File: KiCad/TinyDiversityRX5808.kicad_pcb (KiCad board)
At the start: 2 copper layers, 22 x 19.7 mm, 31 parts, among them J1 Googles, J2 RX_A, J3 RX_B, J4 Conn_01x06, SW1 SW_Push, U1 MAX4624, U2 ATTINY85-20SU

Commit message: Change schottky footprint
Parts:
- D3: footprint Diodes_SMD:D_SOD-523 -> Diodes_SMD:D_SOD-323
- moved D3 0.30 mm to (148.9, 94.9)
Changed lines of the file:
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@@
-    )
-  )
-  (module Diodes_SMD:D_SOD-523 (layer F.Cu)
-    (at 148.65 94.83)
-    (descr "http://www.diodes.com/datasheets/ap02001.pdf p.144")
-    (tags "Diode SOD523")
-    (attr smd)
-    (fp_text reference D3 (at 0 -1.3) (layer F.SilkS) hide
-      (effects (font (size 1 1) (thickness 0.15)))
-    )
-    (fp_text value D_Schottky (at 0 1.4) (layer F.Fab) hide
-      (effects (font (size 1 1) (thickness 0.15)))
-    )
-    (fp_text user %R (at 0 -1.3) (layer F.Fab) hide
-      (effects (font (size 1 1) (thickness 0.15)))
-    )
-    (fp_line (start -1.15 -0.6) (end -1.15 0.6) (layer F.SilkS) (width 0.12))
-    (fp_line (start 1.25 -0.7) (end 1.25 0.7) (layer F.CrtYd) (width 0.05))
-    (fp_line (start -1.25 -0.7) (end 1.25 -0.7) (layer F.CrtYd) (width 0.05))
-    (fp_line (start -1.25 0.7) (end -1.25 -0.7) (layer F.CrtYd) (width 0.05))
-    (fp_line (start 1.25 0.7) (end -1.25 0.7) (layer F.CrtYd) (width 0.05))
-    (fp_line (start 0.1 0) (end 0.25 0) (layer F.Fab) (width 0.1))
-    (fp_line (start 0.1 -0.2) (end -0.2 0) (layer F.Fab) (width 0.1))
-    (fp_line (start 0.1 0.2) (end 0.1 -0.2) (layer F.Fab) (width 0.1))
-    (fp_line (start -0.2 0) (end 0.1 0.2) (layer F.Fab) (width 0.1))
-    (fp_line (start -0.2 0) (end -0.35 0) (layer F.Fab) (width 0.1))
-    (fp_line (start -0.2 0.2) (end -0.2 -0.2) (layer F.Fab) (width 0.1))
-    (fp_line (start 0.65 -0.45) (end 0.65 0.45) (layer F.Fab) (width 0.1))
-    (fp_line (start -0.65 -0.45) (end 0.65 -0.45) (layer F.Fab) (width 0.1))
-    (fp_line (start -0.65 0.45) (end -0.65 -0.45) (layer F.Fab) (width 0.1))
-    (fp_line (start 0.65 0.45) (end -0.65 0.45) (layer F.Fab) (width 0.1))
-    (fp_line (start 0.7 -0.6) (end -1.15 -0.6) (layer F.SilkS) (width 0.12))
-    (fp_line (start 0.7 0.6) (end -1.15 0.6) (layer F.SilkS) (width 0.12))
-    (pad 2 smd rect (at 0.7 0 180) (size 0.6 0.7) (layers F.Cu F.Paste F.Mask)
-      (net 3 VCC))
-    (pad 1 smd rect (at -0.7 0 180) (size 0.6 0.7) (layers F.Cu F.Paste F.Mask)
-      (net 2 /PROG_PWR))
-    (model ${KISYS3DMOD}/Diodes_SMD.3dshapes/D_SOD-523.wrl
-      (at (xyz 0 0 0))
-      (scale (xyz 1 1 1))
-      (rotate (xyz 0 0 0))
     )
   )
@@
       (scale (xyz 1 1 1))
       (rotate (xyz 0 0 180))
+    )
+  )
+  (module Diodes_SMD:D_SOD-323 (layer F.Cu)
+    (at 148.93 94.93)
+    (descr SOD-323)
+    (tags SOD-323)
+    (attr smd)
+    (fp_text reference D3 (at 1.07 -1.43) (layer F.SilkS) hide
+      (effects (font (size 0.6 0.6) (thickness 0.15)))
+    )
+    (fp_text value D_Schottky (at 0.1 1.9) (layer F.Fab) hide
+      (effects (font (size 1 1) (thickness 0.15)))
+    )
+    (fp_text user %R (at 3.14 -0.26) (layer F.Fab) hide
+      (effects (font (size 1 1) (thickness 0.15)))
+    )
+    (fp_line (start -1.5 -0.85) (end -1.5 0.85) (layer F.SilkS) (width 0.12))
+    (fp_line (start 0.2 0) (end 0.45 0) (layer F.Fab) (width 0.1))
+    (fp_line (start 0.2 0.35) (end -0.3 0) (layer F.Fab) (width 0.1))
+    (fp_line (start 0.2 -0.35) (end 0.2 0.35) (layer F.Fab) (width 0.1))
+    (fp_line (start -0.3 0) (end 0.2 -0.35) (layer F.Fab) (width 0.1))
+    (fp_line (start -0.3 0) (end -0.5 0) (layer F.Fab) (width 0.1))
+    (fp_line (start -0.3 -0.35) (end -0.3 0.35) (layer F.Fab) (width 0.1))
+    (fp_line (start -0.9 0.7) (end -0.9 -0.7) (layer F.Fab) (width 0.1))
+    (fp_line (start 0.9 0.7) (end -0.9 0.7) (layer F.Fab) (width 0.1))
+    (fp_line (start 0.9 -0.7) (end 0.9 0.7) (layer F.Fab) (width 0.1))
+    (fp_line (start -0.9 -0.7) (end 0.9 -0.7) (layer F.Fab) (width 0.1))
+    (fp_line (start -1.6 -0.95) (end 1.6 -0.95) (layer F.CrtYd) (width 0.05))
+    (fp_line (start 1.6 -0.95) (end 1.6 0.95) (layer F.CrtYd) (width 0.05))
+    (fp_line (start -1.6 0.95) (end 1.6 0.95) (layer F.CrtYd) (width 0.05))
+    (fp_line (start -1.6 -0.95) (end -1.6 0.95) (layer F.CrtYd) (width 0.05))
+    (fp_line (start -1.5 0.85) (end 1.05 0.85) (layer F.SilkS) (width 0.12))
+    (fp_line (start -1.5 -0.85) (end 1.05 -0.85) (layer F.SilkS) (width 0.12))
+    (pad 1 smd rect (at -1.05 0) (size 0.6 0.45) (layers F.Cu F.Paste F.Mask)
+      (net 2 /PROG_PWR))
+    (pad 2 smd rect (at 1.05 0) (size 0.6 0.45) (layers F.Cu F.Paste F.Mask)
+      (net 3 VCC))
+    (model ${KISYS3DMOD}/Diodes_SMD.3dshapes/D_SOD-323.wrl
+      (at (xyz 0 0 0))
+      (scale (xyz 1 1 1))
+      (rotate (xyz 0 0 0))
     )
   )
@@
   (segment (start 147.925 94.855) (end 147.95 94.83) (width 0.3) (layer F.Cu) (net 2) (status 30))
   (segment (start 136.36 101.67) (end 136.36 100.29) (width 0.3) (layer F.Cu) (net 2) (status 10))
-  (segment (start 148.13 92.85) (end 148.13 92.095) (width 0.3) (layer F.Cu) (net 3) (status C00000))
-  (segment (start 148.13 92.095) (end 148.15 92.075) (width 0.3) (layer F.Cu) (net 3) (status C00000))
-  (segment (start 131.46 92.85) (end 131.46 92.11) (width 0.3) (layer F.Cu) (net 3) (status C00000))
-  (segment (start 131.46 92.11) (end 131.425 92.075) (width 0.3) (layer F.Cu) (net 3) (status C00000))
+  (segment (start 149.98 94.93) (end 149.98 93.43) (width 0.3) (layer F.Cu) (net 3) (status 400000))
+  (segment (start 149.98 93.43) (end 149.4 92.85) (width 0.3) (layer F.Cu) (net 3))
+  (segment (start 148.9 96.53) (end 149.98 95.45) (width 0.3) (layer F.Cu) (net 3))
+  (segment (start 148.9 99.04) (end 148.9 96.53) (width 0.3) (layer F.Cu) (net 3))
+  (segment (start 148.215 99.725) (end 148.9 99.04) (width 0.3) (layer F.Cu) (net 3))
+  (segment (start 147.125 99.725) (end 148.215 99.725) (width 0.3) (layer F.Cu) (net 3))
+  (segment (start 149.98 95.45) (end 149.98 94.93) (width 0.3) (layer F.Cu) (net 3) (status 800000))
+  (segment (start 148.13 92.85) (end 148.13 92.095) (width 0.3) (layer F.Cu) (net 3))
+  (segment (start 148.13 92.095) (end 148.15 92.075) (width 0.3) (layer F.Cu) (net 3))
+  (segment (start 131.46 92.85) (end 131.46 92.11) (width 0.3) (layer F.Cu) (net 3))
+  (segment (start 131.46 92.11) (end 131.425 92.075) (width 0.3) (layer F.Cu) (net 3))
   (segment (start 130.325 99.7) (end 130.325 99.715) (width 0.3) (layer B.Cu) (net 3))
   (via (at 130.325 99.7) (size 1) (drill 0.4) (layers F.Cu B.Cu) (net 3))
@@
   (segment (start 139.95 107.95) (end 144.15 107.95) (width 0.3) (layer B.Cu) (net 3))
   (segment (start 146.25 100.6) (end 147.125 99.725) (width 0.3) (layer B.Cu) (net 3))
-  (segment (start 147.125 99.725) (end 148.215 99.725) (width 0.3) (layer F.Cu) (net 3))
-  (segment (start 148.215 99.725) (end 148.9 99.04) (width 0.3) (layer F.Cu) (net 3))
-  (segment (start 148.9 99.04) (end 148.9 95.85) (width 0.3) (layer F.Cu) (net 3))
-  (segment (start 148.9 95.85) (end 149.35 95.4) (width 0.3) (layer F.Cu) (net 3))
-  (segment (start 149.35 95.4) (end 149.35 94.83) (width 0.3) (layer F.Cu) (net 3))
   (segment (start 139.8 108.1) (end 139.95 107.95) (width 0.3) (layer B.Cu) (net 3))
   (via (at 147.125 99.725) (size 1) (drill 0.4) (layers F.Cu B.Cu) (net 3))
@@
   (segment (start 145.36 106.74) (end 145.36 105.22) (width 0.3) (layer B.Cu) (net 3))
   (segment (start 144.15 107.95) (end 145.36 106.74) (width 0.3) (layer B.Cu) (net 3))
-  (segment (start 149.35 94.83) (end 149.35 92.9) (width 0.3) (layer F.Cu) (net 3))
   (segment (start 149.35 92.9) (end 149.4 92.85) (width 0.3) (layer F.Cu) (net 3))
   (segment (start 148.13 92.85) (end 149.4 92.85) (width 0.3) (layer F.Cu) (net 3))
@@
   (segment (start 130.16 92.86) (end 130.17 92.85) (width 0.3) (layer B.Cu) (net 3))
   (segment (start 130.17 92.85) (end 131.46 92.85) (width 0.3) (layer B.Cu) (net 3))
-  (segment (start 149.35 94.83) (end 149.35 94.975) (width 0.3) (layer F.Cu) (net 3) (status 30))
-  (segment (start 133.66 92.85) (end 133.66 92.115) (width 0.2) (layer F.Cu) (net 4) (status C00000))
-  (segment (start 133.66 92.115) (end 133.7 92.075) (width 0.2) (layer F.Cu) (net 4) (status C00000))
+  (segment (start 133.66 92.85) (end 133.66 92.115) (width 0.2) (layer F.Cu) (net 4))
+  (segment (start 133.66 92.115) (end 133.7 92.075) (width 0.2) (layer F.Cu) (net 4))
   (segment (start 133.66 92.85) (end 133.69 92.88) (width 0.2) (layer B.Cu) (net 4))
   (segment (start 133.69 92.88) (end 133.69 93.5) (width 0.2) (layer B.Cu) (net 4))
@@
   (via (at 133.69 93.5) (size 0.6) (drill 0.3) (layers F.Cu B.Cu) (net 4))
   (segment (start 137.88 97.69) (end 133.69 93.5) (width 0.2) (layer B.Cu) (net 4))
-  (segment (start 145.9 92.075) (end 145.9 92.82) (width 0.2) (layer F.Cu) (net 5) (status C00000))
-  (segment (start 145.9 92.82) (end 145.93 92.85) (width 0.2) (layer F.Cu) (net 5) (status C00000))
+  (segment (start 145.9 92.075) (end 145.9 92.82) (width 0.2) (layer F.Cu) (net 5))
+  (segment (start 145.9 92.82) (end 145.93 92.85) (width 0.2) (layer F.Cu) (net 5))
   (segment (start 145.9 94.23) (end 145.9 93.91) (width 0.2) (layer B.Cu) (net 5))
   (segment (start 142.7 97.43) (end 145.9 94.23) (width 0.2) (layer B.Cu) (net 5))

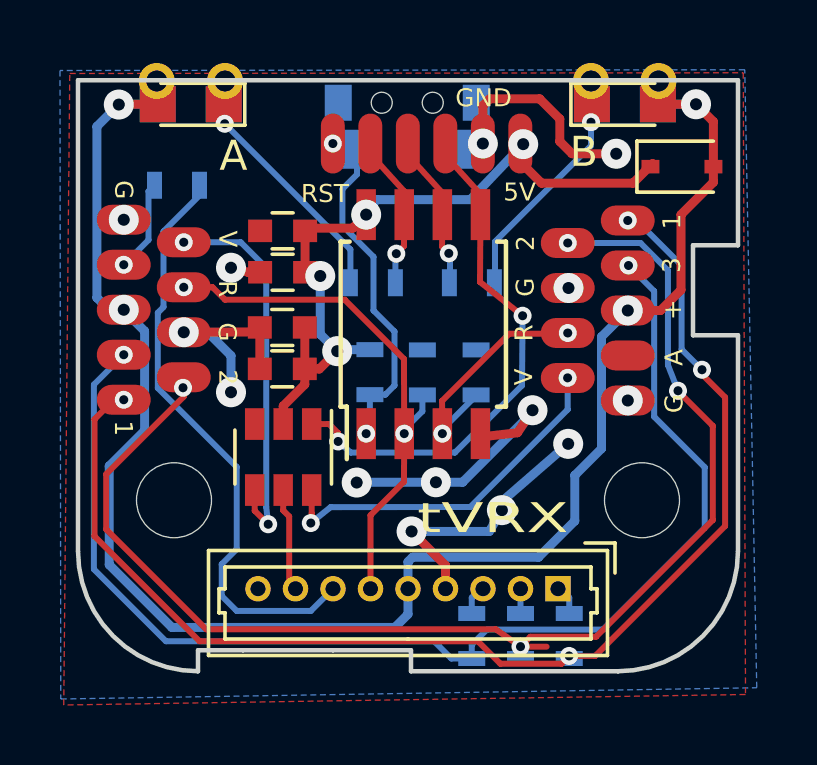
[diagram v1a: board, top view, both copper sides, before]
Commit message: Layout change for easier solder and more thin design
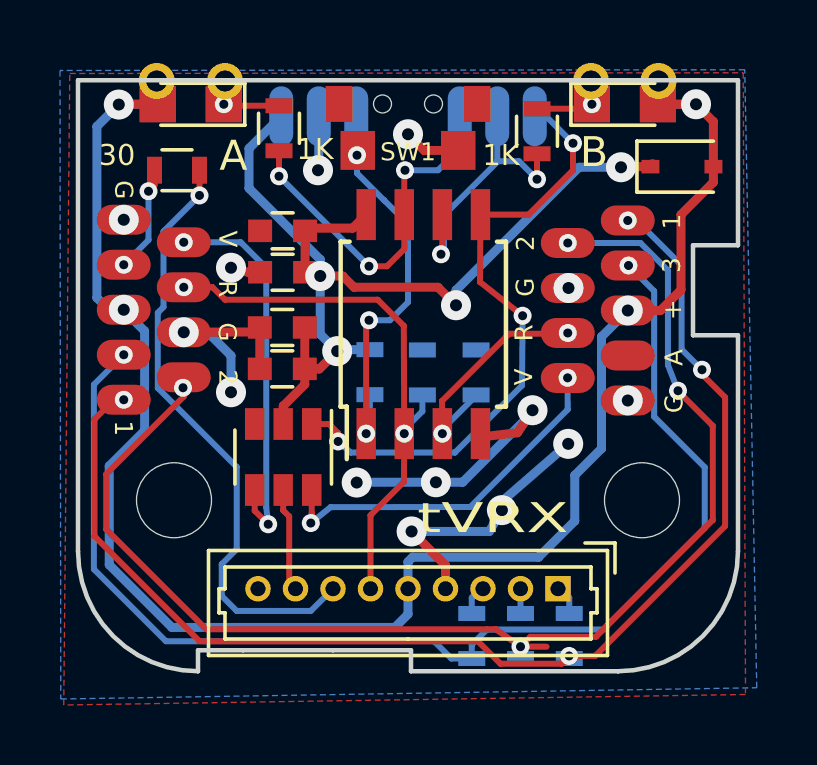
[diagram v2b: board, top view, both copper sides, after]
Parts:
- added J5: Prog2, KiCadCustomLibs:Pads_prog_3pin1.25mm, B.Cu at (142.8, 93.2)
- D3: value D_Schottky -> B5819WS
- J4: value Conn_01x06 -> Prog1; footprint KiCadCustomLibs:Pads_prog_6pin1.25mm -> KiCadCustomLibs:Pads_prog_3pin1.25mm; moved to B.Cu
- R6, R7, R8: moved to F.Cu
- SW1: footprint KiCadCustomLibs:Button_TS-018 -> Button_TS-018; moved to F.Cu
- moved R6 6.03 mm to (135.5, 93.7), turned to 90 degrees
- moved R7 5.50 mm to (144.1, 93.8), turned to 90 degrees
- moved J4 3.73 mm to (136.8, 93.2), turned to 0 degrees
- moved R8 0.50 mm to (132.1, 95.0)
- turned SW1 to 0 degrees
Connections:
- J4 pad 3: /MOSI -> /RST
- SW1 pad 1: GND -> /RST
- SW1 pad 2: /RST -> GND
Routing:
- net /PROG_PWR: track 24.8 -> 33.4 mm
- net /SCK: track 5.19 -> 13.1 mm, vias 1 -> 3
- net Net-(D1-Pad1): track 9.77 -> 2.69 mm
- net Net-(D2-Pad1): track 8.68 -> 2.68 mm
- net /MISO: track 5.19 -> 10.0 mm, vias 1 -> 2
- net /MOSI: track 17.8 -> 21.9 mm, vias 2 -> 3
- net GND: track 34.4 -> 30.6 mm
- net /RST: track 11.9 -> 14.6 mm, vias 2 -> 3
- net /RSSI_A: track 17.9 -> 18.5 mm
- net /AUD_IN: track 19.8 -> 20.3 mm, vias 0 -> 1
- net /AUD_OUT: track 3.07 -> 3.57 mm, vias 1 -> 2
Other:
- board text added: "MISO"
- board text added: "MOSI"
- board text added: "SCK"
- board text removed: "GND"

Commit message: Add panelized PCB (4x4)
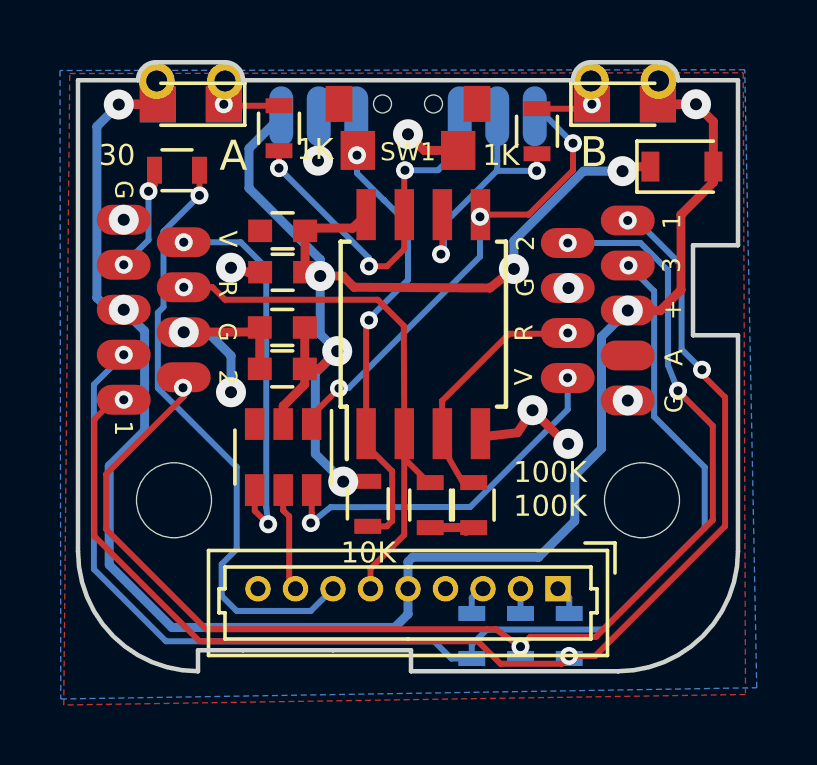
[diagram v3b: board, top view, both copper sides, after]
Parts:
- R4, R5, R9: moved to F.Cu
- moved R4 4.43 mm to (140.5, 106.2), turned to 90 degrees
- moved R5 4.42 mm to (142.0, 106.2), turned to 90 degrees
- moved R9 4.39 mm to (138.5, 106.2)
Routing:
- net GND: track 30.6 -> 17.4 mm, vias 14 -> 10
- net /MOSI: track 21.9 -> 16.5 mm
- net /PROG_PWR: track 33.4 -> 37.9 mm, vias 4 -> 5
- net /RST: track 14.6 -> 17.1 mm, vias 3 -> 2
- net Net-(J2-Pad2): track 44.1 -> 43.2 mm
- net /RSSI_A: track 18.5 -> 19.1 mm, vias 2 -> 1
- net /RSSI_B: track 7.87 -> 8.41 mm, vias 2 -> 1
- net /MISO: track 10.0 -> 9.49 mm
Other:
- board size 22 x 19.7 mm -> 22 x 20.3 mm
- board text added: "100K 100K"
- board text added: "GND"
- board text removed: "100K"
